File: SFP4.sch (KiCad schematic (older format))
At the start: 19 parts, among them J8 TYCO_1888247-1

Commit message: Convert all footprints to use Marble nickname
Includes both .sch and .lib files
Includes both bare footprint names and those with CERN-like nicknames
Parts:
- C100, C101, C94, C98: footprint CAPC0603X33N -> Marble:CAPC0603X33N
- C95, C97: footprint CAPC1005X55N -> Marble:CAPC1005X55N
- C96, C99: footprint CAPC1608X87N -> Marble:CAPC1608X87N
- L7, L8: footprint INDC1608X65N -> Marble:INDC1608X65N
- R186, R187, R85, R86, R87, R88, R89, R90: footprint RESC1005X40N -> Marble:RESC1005X40N
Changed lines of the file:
@@
 F 0 "R187" V 7854 3910 50  0000 L CNN
 F 1 "R0402_10K_1%_0.0625W_100PPM" H 7750 3640 60  0001 L CNN
-F 2 "RESC1005X40N" H 7750 2830 60  0001 L CNN
+F 2 "Marble:RESC1005X40N" H 7750 2830 60  0001 L CNN
 F 3 "\\\\cern.ch\\dfs\\Applications\\Altium\\Datasheets\\R0402_Phycomp_RC0402.pdf" H 7750 3460 60  0001 L CNN
 F 4 "10k" V 7945 3910 50  0000 L CNN "~"
@@
 F 0 "R90" V 7554 2710 50  0000 L CNN
 F 1 "R0402_10K_1%_0.0625W_100PPM" H 7450 2440 60  0001 L CNN
-F 2 "RESC1005X40N" H 7450 1630 60  0001 L CNN
+F 2 "Marble:RESC1005X40N" H 7450 1630 60  0001 L CNN
 F 3 "\\\\cern.ch\\dfs\\Applications\\Altium\\Datasheets\\R0402_Phycomp_RC0402.pdf" H 7450 2260 60  0001 L CNN
 F 4 "10k" V 7645 2710 50  0000 L CNN "~"
@@
 F 0 "R186" V 7804 2710 50  0000 L CNN
 F 1 "R0402_10K_1%_0.0625W_100PPM" H 7700 2440 60  0001 L CNN
-F 2 "RESC1005X40N" H 7700 1630 60  0001 L CNN
+F 2 "Marble:RESC1005X40N" H 7700 1630 60  0001 L CNN
 F 3 "\\\\cern.ch\\dfs\\Applications\\Altium\\Datasheets\\R0402_Phycomp_RC0402.pdf" H 7700 2260 60  0001 L CNN
 F 4 "10k" V 7895 2710 50  0000 L CNN "~"
@@
 F 0 "C94" V 1254 2060 50  0000 L CNN
 F 1 "CC0201_100NF_6.3V_10%_X5R" H 1150 1690 60  0001 L CNN
-F 2 "CAPC0603X33N" H 1150 880 60  0001 L CNN
+F 2 "Marble:CAPC0603X33N" H 1150 880 60  0001 L CNN
 F 3 "\\\\cern.ch\\dfs\\Applications\\Altium\\Datasheets\\CC0201_X5R_AVX.pdf" H 1150 1510 60  0001 L CNN
 F 4 "100nF" V 1345 2060 50  0000 L CNN "~"
@@
 F 0 "C98" V 3204 2060 50  0000 L CNN
 F 1 "CC0201_100NF_6.3V_10%_X5R" H 3100 1690 60  0001 L CNN
-F 2 "CAPC0603X33N" H 3100 880 60  0001 L CNN
+F 2 "Marble:CAPC0603X33N" H 3100 880 60  0001 L CNN
 F 3 "\\\\cern.ch\\dfs\\Applications\\Altium\\Datasheets\\CC0201_X5R_AVX.pdf" H 3100 1510 60  0001 L CNN
 F 4 "100nF" V 3295 2060 50  0000 L CNN "~"
@@
 F 0 "C100" V 3604 2060 50  0000 L CNN
 F 1 "CC0201_100NF_6.3V_10%_X5R" H 3500 1690 60  0001 L CNN
-F 2 "CAPC0603X33N" H 3500 880 60  0001 L CNN
+F 2 "Marble:CAPC0603X33N" H 3500 880 60  0001 L CNN
 F 3 "\\\\cern.ch\\dfs\\Applications\\Altium\\Datasheets\\CC0201_X5R_AVX.pdf" H 3500 1510 60  0001 L CNN
 F 4 "100nF" V 3695 2060 50  0000 L CNN "~"
@@
 F 0 "C101" V 3954 3060 50  0000 L CNN
 F 1 "CC0201_100NF_6.3V_10%_X5R" H 3850 2690 60  0001 L CNN
-F 2 "CAPC0603X33N" H 3850 1880 60  0001 L CNN
+F 2 "Marble:CAPC0603X33N" H 3850 1880 60  0001 L CNN
 F 3 "\\\\cern.ch\\dfs\\Applications\\Altium\\Datasheets\\CC0201_X5R_AVX.pdf" H 3850 2510 60  0001 L CNN
 F 4 "100nF" V 4045 3060 50  0000 L CNN "~"
@@
 F 0 "L7" H 2000 2167 50  0000 C CNN
 F 1 "IND0603_MURATA_BLM18SG121TN1D" H 1850 1760 60  0001 L CNN
-F 2 "INDC1608X65N" H 1850 950 60  0001 L CNN
+F 2 "Marble:INDC1608X65N" H 1850 950 60  0001 L CNN
 F 3 "\\\\cern.ch\\dfs\\Applications\\Altium\\Datasheets\\IND0603_MURATA_BLM18S.pdf" H 1850 1580 60  0001 L CNN
 F 4 "120R@100MHz" H 2000 2076 50  0000 C CNN "~"
@@
 F 0 "L8" H 3250 3167 50  0000 C CNN
 F 1 "IND0603_MURATA_BLM18SG121TN1D" H 3100 2760 60  0001 L CNN
-F 2 "INDC1608X65N" H 3100 1950 60  0001 L CNN
+F 2 "Marble:INDC1608X65N" H 3100 1950 60  0001 L CNN
 F 3 "\\\\cern.ch\\dfs\\Applications\\Altium\\Datasheets\\IND0603_MURATA_BLM18S.pdf" H 3100 2580 60  0001 L CNN
 F 4 "120R@100MHz" H 3250 3076 50  0000 C CNN "~"
@@
 F 0 "C95" V 1704 2060 50  0000 L CNN
 F 1 "CC0402_1UF_16V_10%_X5R" H 1600 1690 60  0001 L CNN
-F 2 "CAPC1005X55N" H 1600 880 60  0001 L CNN
+F 2 "Marble:CAPC1005X55N" H 1600 880 60  0001 L CNN
 F 3 "\\\\cern.ch\\dfs\\Applications\\Altium\\Datasheets\\CC0402_X5R_TDK_C.pdf" H 1600 1510 60  0001 L CNN
 F 4 "1uF" V 1795 2060 50  0000 L CNN "~"
@@
 F 0 "C97" V 2804 2060 50  0000 L CNN
 F 1 "CC0402_1UF_16V_10%_X5R" H 2700 1690 60  0001 L CNN
-F 2 "CAPC1005X55N" H 2700 880 60  0001 L CNN
+F 2 "Marble:CAPC1005X55N" H 2700 880 60  0001 L CNN
 F 3 "\\\\cern.ch\\dfs\\Applications\\Altium\\Datasheets\\CC0402_X5R_TDK_C.pdf" H 2700 1510 60  0001 L CNN
 F 4 "1uF" V 2895 2060 50  0000 L CNN "~"
@@
 F 0 "C96" V 2496 2140 50  0000 R CNN
 F 1 "CC0603_10UF_6.3V_20%_X5R" H 2300 1990 60  0001 L CNN
-F 2 "CAPC1608X87N" H 2300 1180 60  0001 L CNN
+F 2 "Marble:CAPC1608X87N" H 2300 1180 60  0001 L CNN
 F 3 "\\\\cern.ch\\dfs\\Applications\\Altium\\Datasheets\\CC0603_X5R_KEMET.pdf" H 2300 1810 60  0001 L CNN
 F 4 "10uF" V 2405 2140 50  0000 R CNN "~"
@@
 F 0 "C99" V 3646 3140 50  0000 R CNN
 F 1 "CC0603_10UF_6.3V_20%_X5R" H 3450 2990 60  0001 L CNN
-F 2 "CAPC1608X87N" H 3450 2180 60  0001 L CNN
+F 2 "Marble:CAPC1608X87N" H 3450 2180 60  0001 L CNN
 F 3 "\\\\cern.ch\\dfs\\Applications\\Altium\\Datasheets\\CC0603_X5R_KEMET.pdf" H 3450 2810 60  0001 L CNN
 F 4 "10uF" V 3555 3140 50  0000 R CNN "~"
@@
 F 0 "R89" V 7304 2710 50  0000 L CNN
 F 1 "R0402_10K_1%_0.0625W_100PPM" H 7200 2440 60  0001 L CNN
-F 2 "RESC1005X40N" H 7200 1630 60  0001 L CNN
+F 2 "Marble:RESC1005X40N" H 7200 1630 60  0001 L CNN
 F 3 "\\\\cern.ch\\dfs\\Applications\\Altium\\Datasheets\\R0402_Phycomp_RC0402.pdf" H 7200 2260 60  0001 L CNN
 F 4 "10k" V 7395 2710 50  0000 L CNN "~"
@@
 F 0 "R88" V 7054 2710 50  0000 L CNN
 F 1 "R0402_10K_1%_0.0625W_100PPM" H 6950 2440 60  0001 L CNN
-F 2 "RESC1005X40N" H 6950 1630 60  0001 L CNN
+F 2 "Marble:RESC1005X40N" H 6950 1630 60  0001 L CNN
 F 3 "\\\\cern.ch\\dfs\\Applications\\Altium\\Datasheets\\R0402_Phycomp_RC0402.pdf" H 6950 2260 60  0001 L CNN
 F 4 "10k" V 7145 2710 50  0000 L CNN "~"
@@
 F 0 "R87" V 6804 2710 50  0000 L CNN
 F 1 "R0402_10K_1%_0.0625W_100PPM" H 6700 2440 60  0001 L CNN
-F 2 "RESC1005X40N" H 6700 1630 60  0001 L CNN
+F 2 "Marble:RESC1005X40N" H 6700 1630 60  0001 L CNN
 F 3 "\\\\cern.ch\\dfs\\Applications\\Altium\\Datasheets\\R0402_Phycomp_RC0402.pdf" H 6700 2260 60  0001 L CNN
 F 4 "10k" V 6895 2710 50  0000 L CNN "~"
@@
 F 0 "R85" H 6250 3703 50  0000 C CNN
 F 1 "R0402_10K_1%_0.0625W_100PPM" H 6100 3690 60  0001 L CNN
-F 2 "RESC1005X40N" H 6100 2880 60  0001 L CNN
+F 2 "Marble:RESC1005X40N" H 6100 2880 60  0001 L CNN
 F 3 "\\\\cern.ch\\dfs\\Applications\\Altium\\Datasheets\\R0402_Phycomp_RC0402.pdf" H 6100 3510 60  0001 L CNN
 F 4 "10k" H 6250 3794 50  0000 C CNN "~"
@@
 F 0 "R86" V 6354 3960 50  0000 L CNN
 F 1 "R0402_0R_JUMPER" H 6250 3690 60  0001 L CNN
-F 2 "RESC1005X40N" H 6250 2880 60  0001 L CNN
+F 2 "Marble:RESC1005X40N" H 6250 2880 60  0001 L CNN
 F 3 "\\\\cern.ch\\dfs\\Applications\\Altium\\Datasheets\\R0402_Phycomp_RC0402.pdf" H 6250 3510 60  0001 L CNN
 F 4 "0" V 6445 3960 50  0000 L CNN "~"

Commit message: mark SFP TX_DIS pulldown resistors as 0 Ohm DNF
R84 R105 R185 R187
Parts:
- R187: value R0402_10K_1%_0.0625W_100PPM -> R0402_0R_JUMPER; symbol Resistors_SMD:R0402_10K_1%_0.0625W_100PPM -> Resistors_SMD:R0402_0R_JUMPER; Comment =Value -> 0; ComponentHeight ~~ -> (none); Database Table Name (none) -> Resistors SMD; Footprint Library (none) -> Resistors SMD; Library Name Resistors SMD -> Resistors.DbLib; Library Ref Resistor - 1% -> Resistor; Manufacturer Part Number R0402_10K_1%_0.0625W_100PPM -> R0402_0R_JUMPER; Manufacturer1 Part Number 232270671003L -> 232270591001L; PackageDescription ~~ -> (none); Part Description General Purpose Thick Film Chip Resistor -> 1A (0.05R Max DC Resistance) Zero Ohm Jumper; Part Number R0402_10K_1%_0.0625W_100PPM -> R0402_0R_JUMPER; Power 0.0625W -> (none); Sense Comment ~~ -> (none); Status Comment ~~ -> (none); TC ±100ppm/°C -> (none); Tolerance ±1% -> (none); Val 10k -> 0; Voltage ~~ -> (none); ~ 10k -> DNP
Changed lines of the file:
@@
 SFP4_RS
 $Comp
-L Resistors_SMD:R0402_10K_1%_0.0625W_100PPM R?
+L Resistors_SMD:R0402_0R_JUMPER R?
 U 1 1 5C65B435
 P 7750 3850
@@
 AR Path="/5CC8AFE1/5C65B435" Ref="R187"  Part="1"
 F 0 "R187" V 7854 3910 50  0000 L CNN
-F 1 "R0402_10K_1%_0.0625W_100PPM" H 7750 3640 60  0001 L CNN
+F 1 "R0402_0R_JUMPER" H 7750 3640 60  0001 L CNN
 F 2 "Marble:RESC1005X40N" H 7750 2830 60  0001 L CNN
 F 3 "\\\\cern.ch\\dfs\\Applications\\Altium\\Datasheets\\R0402_Phycomp_RC0402.pdf" H 7750 3460 60  0001 L CNN
-F 4 "10k" V 7945 3910 50  0000 L CNN "~"
-F 5 "R0402_10K_1%_0.0625W_100PPM" H 7750 3370 60  0001 L CNN "Part Number"
-F 6 "Resistor - 1%" H 7750 3280 60  0001 L CNN "Library Ref"
+F 4 "DNP" V 7945 3910 50  0000 L CNN "~"
+F 5 "R0402_0R_JUMPER" H 7750 3370 60  0001 L CNN "Part Number"
+F 6 "Resistor" H 7750 3280 60  0001 L CNN "Library Ref"
 F 7 "SchLib\\Resistors.SchLib" H 7750 3190 60  0001 L CNN "Library Path"
-F 8 "=Value" H 7750 3100 60  0001 L CNN "Comment"
+F 8 "0" H 7750 3100 60  0001 L CNN "Comment"
 F 9 "Standard" H 7750 3010 60  0001 L CNN "Component Kind"
 F 10 "Standard" H 7750 2920 60  0001 L CNN "Component Type"
-F 11 "~~" H 7750 2740 60  0001 L CNN "PackageDescription"
+F 11 " " H 7750 2740 60  0001 L CNN "PackageDescription"
 F 12 "2" H 7750 2650 60  0001 L CNN "Pin Count"
 F 13 "PcbLib\\Resistors SMD.PcbLib" H 7750 2560 60  0001 L CNN "Footprint Path"
 F 14 "RESC1005X40N" H 7750 2470 60  0001 L CNN "Footprint Ref"
-F 15 "10k" H 7750 2380 60  0001 L CNN "Val"
+F 15 "0" H 7750 2380 60  0001 L CNN "Val"
 F 16 "Not Recommended" H 7750 2290 60  0001 L CNN "Status"
-F 17 "0.0625W" H 7750 2200 60  0001 L CNN "Power"
-F 18 "±100ppm/°C" H 7750 2110 60  0001 L CNN "TC"
-F 19 "~~" H 7750 2020 60  0001 L CNN "Voltage"
-F 20 "±1%" H 7750 1930 60  0001 L CNN "Tolerance"
-F 21 "General Purpose Thick Film Chip Resistor" H 7750 1840 60  0001 L CNN "Part Description"
+F 17 " " H 7750 2200 60  0001 L CNN "Power"
+F 18 " " H 7750 2110 60  0001 L CNN "TC"
+F 19 " " H 7750 2020 60  0001 L CNN "Voltage"
+F 20 " " H 7750 1930 60  0001 L CNN "Tolerance"
+F 21 "1A (0.05R Max DC Resistance) Zero Ohm Jumper" H 7750 1840 60  0001 L CNN "Part Description"
 F 22 "GENERIC" H 7750 1750 60  0001 L CNN "Manufacturer"
-F 23 "R0402_10K_1%_0.0625W_100PPM" H 7750 1660 60  0001 L CNN "Manufacturer Part Number"
+F 23 "R0402_0R_JUMPER" H 7750 1660 60  0001 L CNN "Manufacturer Part Number"
 F 24 "0402" H 7750 1570 60  0001 L CNN "Case"
 F 25 "No" H 7750 1480 60  0001 L CNN "PressFit"
 F 26 "Yes" H 7750 1390 60  0001 L CNN "Mounted"
-F 27 "~~" H 7750 1300 60  0001 L CNN "Sense Comment"
+F 27 " " H 7750 1300 60  0001 L CNN "Sense Comment"
 F 28 "No" H 7750 1210 60  0001 L CNN "Sense"
-F 29 "~~" H 7750 1120 60  0001 L CNN "Status Comment"
+F 29 " " H 7750 1120 60  0001 L CNN "Status Comment"
 F 30 "No" H 7750 1030 60  0001 L CNN "Socket"
 F 31 "Yes" H 7750 940 60  0001 L CNN "SMD"
-F 32 "~~" H 7750 850 60  0001 L CNN "ComponentHeight"
+F 32 " " H 7750 850 60  0001 L CNN "ComponentHeight"
 F 33 "YAGEO PHYCOMP" H 7750 760 60  0001 L CNN "Manufacturer1 Example"
-F 34 "232270671003L" H 7750 670 60  0001 L CNN "Manufacturer1 Part Number"
+F 34 "232270591001L" H 7750 670 60  0001 L CNN "Manufacturer1 Part Number"
 F 35 "0.4mm" H 7750 580 60  0001 L CNN "Manufacturer1 ComponentHeight"
 F 36 "\\\\cern.ch\\dfs\\Applications\\Altium\\Datasheets\\R0402_Phycomp_RC0402.pdf" H 7750 490 60  0001 L CNN "HelpURL"
@@
 F 38 "12/03/07 00:00:00" H 7750 310 60  0001 L CNN "CreateDate"
 F 39 "10/17/12 00:00:00" H 7750 220 60  0001 L CNN "LatestRevisionDate"
-F 40 "Resistors SMD" H 7750 130 60  0001 L CNN "Library Name"
+F 40 "Resistors.DbLib" H 7750 130 60  0001 L CNN "Library Name"
 F 41 "This work is licensed under the Creative Commons CC-BY-SA 4.0 License. To the extent that circuit schematics that use Licensed Material can be considered to be ‘Adapted Material’, then the copyright holder waives article 3.b of the license with respect to these schematics." H 7750 40  60  0001 L CNN "License"
+F 42 "Resistors SMD" H 7750 3850 50  0001 C CNN "Database Table Name"
+F 43 "Resistors SMD" H 7750 3850 50  0001 C CNN "Footprint Library"
 	1    7750 3850
 	0    1    1    0

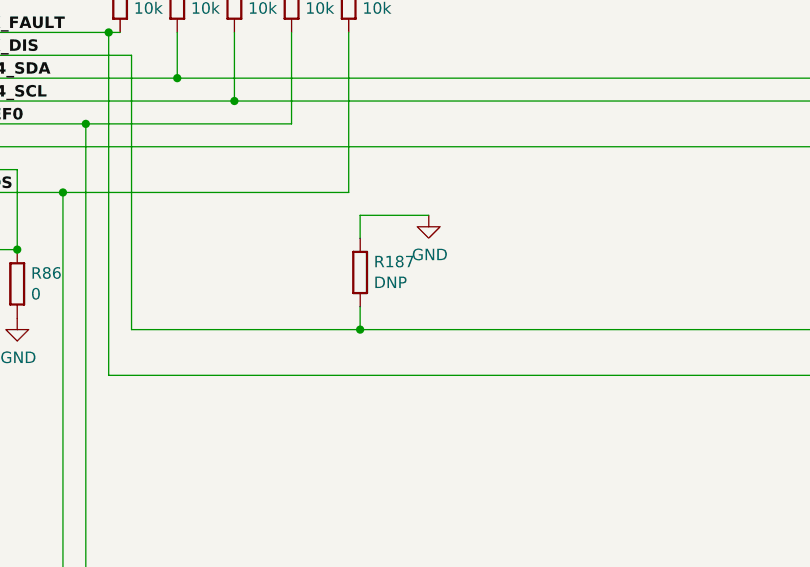
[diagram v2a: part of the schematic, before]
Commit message: Mark R84 R105 R185 R187 dnf in a way that KiBom understands
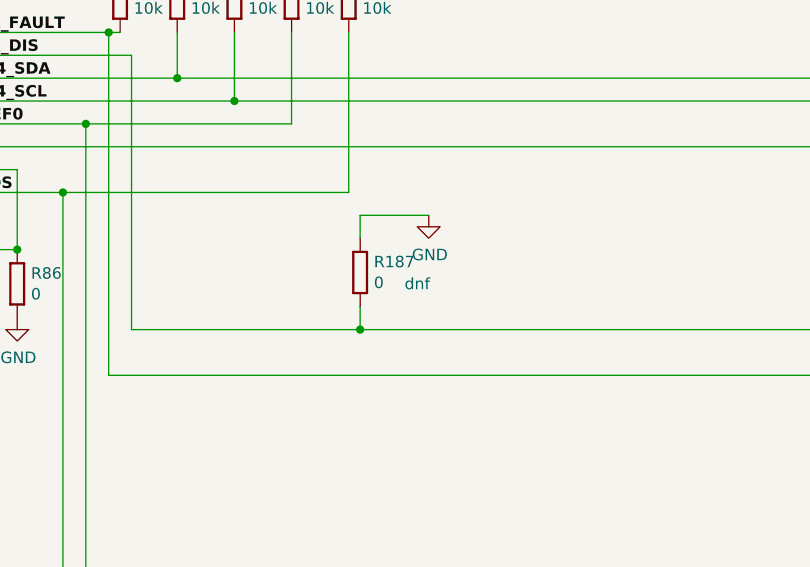
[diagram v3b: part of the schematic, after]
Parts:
- R187: config (none) -> dnf; ~ DNP -> 0
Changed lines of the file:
@@
 F 2 "Marble:RESC1005X40N" H 7750 2830 60  0001 L CNN
 F 3 "\\\\cern.ch\\dfs\\Applications\\Altium\\Datasheets\\R0402_Phycomp_RC0402.pdf" H 7750 3460 60  0001 L CNN
-F 4 "DNP" V 7945 3910 50  0000 L CNN "~"
+F 4 "0" V 7945 3910 50  0000 L CNN "~"
 F 5 "R0402_0R_JUMPER" H 7750 3370 60  0001 L CNN "Part Number"
 F 6 "Resistor" H 7750 3280 60  0001 L CNN "Library Ref"
@@
 F 42 "Resistors SMD" H 7750 3850 50  0001 C CNN "Database Table Name"
 F 43 "Resistors SMD" H 7750 3850 50  0001 C CNN "Footprint Library"
+F 44 "dnf" V 7950 4100 50  0000 C CNN "config"
 	1    7750 3850
 	0    1    1    0

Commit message: Get rid of most .DbLib suffixes in Library Name attributes
Enough that KiBoM no longer complains about them
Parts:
- R187: Library Name Resistors.DbLib -> Resistors SMD
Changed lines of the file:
@@
 F 38 "12/03/07 00:00:00" H 7750 310 60  0001 L CNN "CreateDate"
 F 39 "10/17/12 00:00:00" H 7750 220 60  0001 L CNN "LatestRevisionDate"
-F 40 "Resistors.DbLib" H 7750 130 60  0001 L CNN "Library Name"
+F 40 "Resistors SMD" H 7750 130 60  0001 L CNN "Library Name"
 F 41 "This work is licensed under the Creative Commons CC-BY-SA 4.0 License. To the extent that circuit schematics that use Licensed Material can be considered to be ‘Adapted Material’, then the copyright holder waives article 3.b of the license with respect to these schematics." H 7750 40  60  0001 L CNN "License"
 F 42 "Resistors SMD" H 7750 3850 50  0001 C CNN "Database Table Name"

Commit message: Get rid of more useless inconsistencies in Comment attributes
Makes for quieter KiBoM runs
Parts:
- R187: Comment 0 -> =Value
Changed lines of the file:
@@
 F 6 "Resistor" H 7750 3280 60  0001 L CNN "Library Ref"
 F 7 "SchLib\\Resistors.SchLib" H 7750 3190 60  0001 L CNN "Library Path"
-F 8 "0" H 7750 3100 60  0001 L CNN "Comment"
+F 8 "=Value" H 7750 3100 60  0001 L CNN "Comment"
 F 9 "Standard" H 7750 3010 60  0001 L CNN "Component Kind"
 F 10 "Standard" H 7750 2920 60  0001 L CNN "Component Type"

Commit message: Get rid of "~" attribute in instances
This makes instances line up better with our library
Use a very short python program to rename "~" to "Val" and remove the old "Val".
Required a little pre-patch to correctly handle R297 R298 R299 R300 R162 R274 R197 R198, which had no "~" field.
No net changes to "Val" field contents.
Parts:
- C100, C101, C94, C98: ~ 100nF -> (none)
- C95, C97: ~ 1uF -> (none)
- C96, C99: ~ 10uF -> (none)
- J8: Val (none) -> SFP+; ~ SFP+ -> (none)
- L7, L8: ~ 120R@100MHz -> (none)
- R186, R85, R87, R88, R89, R90: ~ 10k -> (none)
- R187, R86: ~ 0 -> (none)
